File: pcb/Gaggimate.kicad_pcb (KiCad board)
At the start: 2 copper layers, 85 x 67 mm, 107 parts, among them J1 USB_C_Receptacle, J10 Conn_01x02, J2 Conn_01x02, J3 Conn_01x03, J4 Conn_01x04, J5 Conn_01x04, J6 Conn_01x10, J7 Conn_01x02, J8 Conn_01x02, J9 Conn_01x04, K1 Relay_SPDT, K2 Relay_SPDT, K3 Relay_SPDT, Q1 MMBT2222A, Q2 MMBT2222A, Q3 MMBT2222A, SW1 SW_Push, SW2 SW_Push, U1 ESP32-S3-WROOM-1, U2 AMS1117-3.3, U3 USBLC6-2SC6, U6 MAX31855EASA

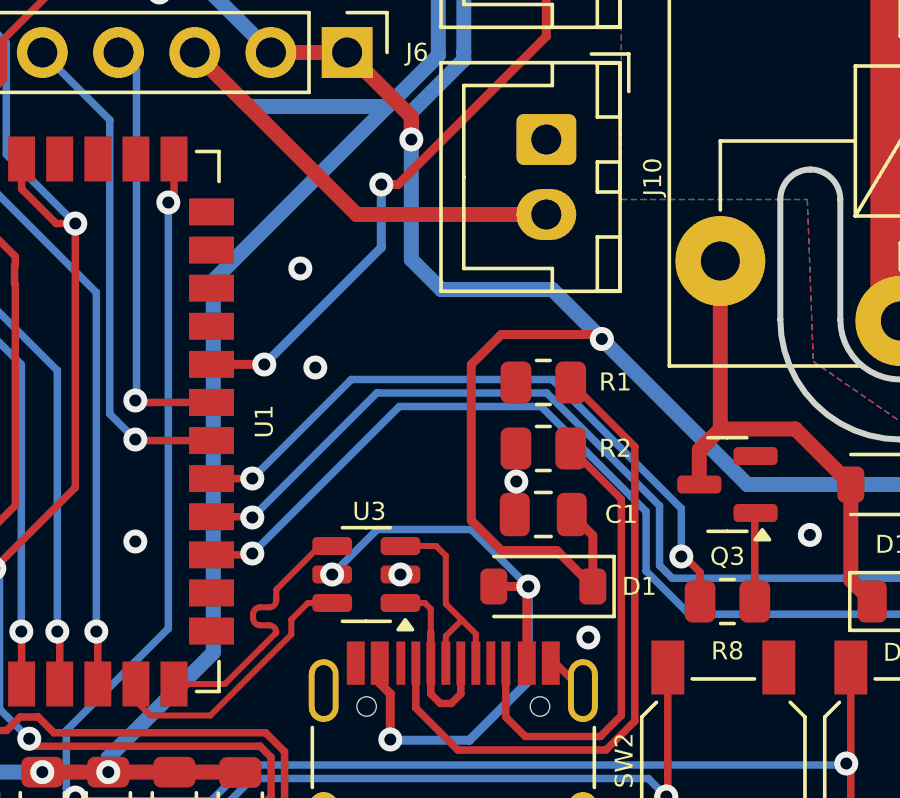
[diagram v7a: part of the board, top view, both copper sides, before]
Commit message: feat: Add expansion mounting hole to PCB, add expansion template
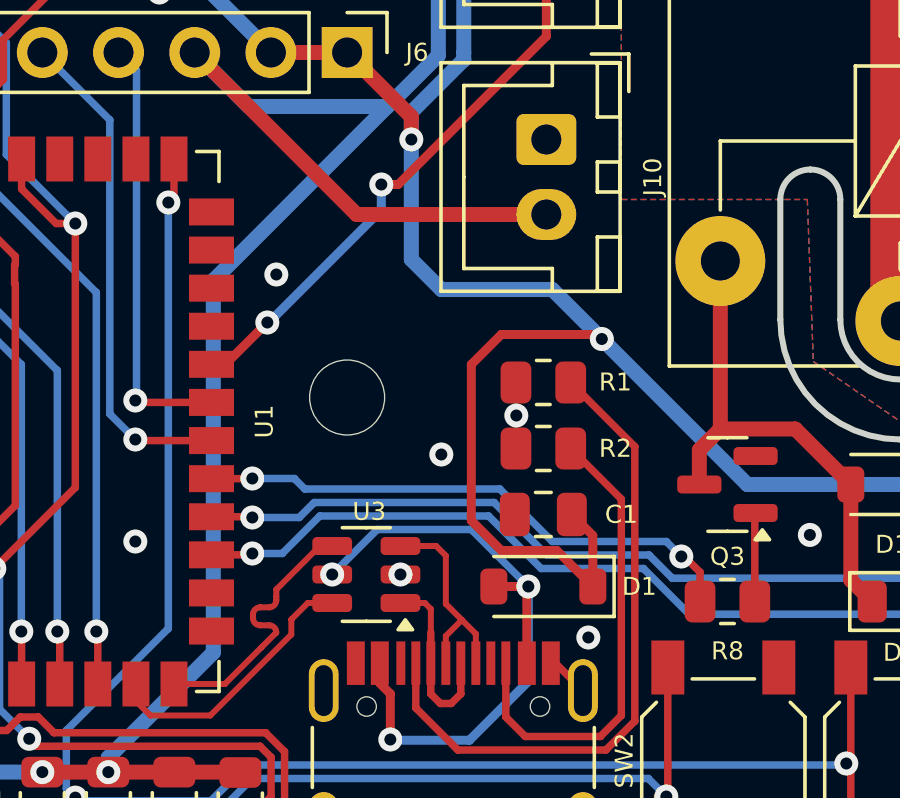
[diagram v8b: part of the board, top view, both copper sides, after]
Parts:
- added REF**: MountingHole_2.5mm, MountingHole:MountingHole_2.5mm, F.Cu at (186.9, 76.6)
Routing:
- net /RELAY_PUMP: track 57.1 -> 53.0 mm
- net /RELAY_VALVE: track 39.6 -> 35.4 mm
- net /RELAY_GRINDER: track 22.3 -> 18.7 mm
- net /SSR: track 19.8 -> 19.0 mm
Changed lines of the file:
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@@
 	(net 71 "unconnected-(D6-K-Pad1)")
 	(net 72 "Net-(K1-PadA1)")
+	(footprint "MountingHole:MountingHole_2.5mm"
+		(layer "F.Cu")
+		(at 186.86 76.6)
+		(descr "Mounting Hole 2.5mm, no annular")
+		(tags "mounting hole 2.5mm no annular")
+		(property "Reference" "REF**"
+			(at 0 -3.5 0)
+			(layer "F.SilkS")
+			(hide yes)
+			(effects
+				(font
+					(size 1 1)
+					(thickness 0.15)
+				)
+			)
+		)
+		(property "Value" "MountingHole_2.5mm"
+			(at 0 3.5 0)
+			(layer "F.Fab")
+			(hide yes)
+			(effects
+				(font
+					(size 1 1)
+					(thickness 0.15)
+				)
+			)
+		)
+		(property "Footprint" "MountingHole:MountingHole_2.5mm"
+			(at 0 0 0)
+			(unlocked yes)
+			(layer "F.Fab")
+			(hide yes)
+			(effects
+				(font
+					(size 1.27 1.27)
+					(thickness 0.15)
+				)
+			)
+		)
+		(property "Datasheet" ""
+			(at 0 0 0)
+			(unlocked yes)
+			(layer "F.Fab")
+			(hide yes)
+			(effects
+				(font
+					(size 1.27 1.27)
+					(thickness 0.15)
+				)
+			)
+		)
+		(property "Description" ""
+			(at 0 0 0)
+			(unlocked yes)
+			(layer "F.Fab")
+			(hide yes)
+			(effects
+				(font
+					(size 1.27 1.27)
+					(thickness 0.15)
+				)
+			)
+		)
+		(attr exclude_from_pos_files exclude_from_bom)
+		(fp_circle
+			(center 0 0)
+			(end 2.75 0)
+			(stroke
+				(width 0.05)
+				(type solid)
+			)
+			(fill none)
+			(layer "F.CrtYd")
+		)
+		(fp_text user "${REFERENCE}"
+			(at 0 0 0)
+			(layer "F.Fab")
+			(effects
+				(font
+					(size 1 1)
+					(thickness 0.15)
+				)
+			)
+		)
+		(pad "" np_thru_hole circle
+			(at 0 0)
+			(size 2.5 2.5)
+			(drill 2.5)
+			(layers "*.Cu" "*.Mask")
+		)
+	)
 	(footprint "Button_Switch_SMD:SW_SPST_SKQG_WithStem"
 		(layer "F.Cu")
@@
 			)
 		)
+		(property "LCSC" "C916372"
+			(at 0 0 180)
+			(unlocked yes)
+			(layer "F.Fab")
+			(hide yes)
+			(effects
+				(font
+					(size 1 1)
+					(thickness 0.15)
+				)
+			)
+		)
 		(property ki_fp_filters "SOT?23*")
 		(sheetname "Root")
@@
 			)
 		)
+		(property "LCSC" "C916372"
+			(at 0 0 180)
+			(unlocked yes)
+			(layer "F.Fab")
+			(hide yes)
+			(effects
+				(font
+					(size 1 1)
+					(thickness 0.15)
+				)
+			)
+		)
 		(property ki_fp_filters "SOT?23*")
 		(sheetname "Root")
@@
 			)
 		)
+		(property "LCSC" "C916372"
+			(at 0 0 180)
+			(unlocked yes)
+			(layer "F.Fab")
+			(hide yes)
+			(effects
+				(font
+					(size 1 1)
+					(thickness 0.15)
+				)
+			)
+		)
 		(property ki_fp_filters "SOT?23*")
 		(sheetname "Root")
@@
 	)
 	(via
-		(at 192.5 79.4)
+		(at 192.5 77.2)
 		(size 0.8)
 		(drill 0.4)
@@
 	)
 	(via
-		(at 185.8 75.6)
+		(at 190 78.5)
 		(size 0.8)
 		(drill 0.4)
@@
 	)
 	(via
-		(at 185.3 72.3)
+		(at 184.5 72.5)
 		(size 0.8)
 		(drill 0.4)
@@
 	)
 	(segment
-		(start 198.263299 83.825)
-		(end 228.775 83.825)
+		(start 228.775 83.825)
+		(end 230.7 81.9)
 		(width 0.25)
 		(layer "B.Cu")
@@
 	)
 	(segment
-		(start 196.825 80.397792)
-		(end 196.825 82.386701)
+		(start 183.7 81.8)
+		(end 184.7 81.8)
 		(width 0.25)
 		(layer "B.Cu")
@@
 	)
 	(segment
-		(start 188.6 76.9)
-		(end 193.327208 76.9)
+		(start 184.7 81.8)
+		(end 185.95 80.55)
 		(width 0.25)
 		(layer "B.Cu")
@@
 	)
 	(segment
-		(start 193.327208 76.9)
-		(end 196.825 80.397792)
+		(start 198.263299 83.825)
+		(end 228.775 83.825)
 		(width 0.25)
 		(layer "B.Cu")
@@
 	)
 	(segment
-		(start 183.7 81.8)
-		(end 188.6 76.9)
+		(start 191.575305 80.55)
+		(end 193.325305 82.3)
 		(width 0.25)
 		(layer "B.Cu")
@@
 	)
 	(segment
-		(start 196.825 82.386701)
+		(start 196.738299 82.3)
 		(end 198.263299 83.825)
 		(width 0.25)
@@
 	)
 	(segment
-		(start 228.775 83.825)
-		(end 230.7 81.9)
+		(start 185.95 80.55)
+		(end 191.575305 80.55)
+		(width 0.25)
+		(layer "B.Cu")
+		(net 23)
+	)
+	(segment
+		(start 193.325305 82.3)
+		(end 196.738299 82.3)
 		(width 0.25)
 		(layer "B.Cu")
@@
 	)
 	(segment
-		(start 197.275 80.211396)
-		(end 197.275 82.200305)
+		(start 197.699695 82.625)
+		(end 213.675 82.625)
 		(width 0.25)
 		(layer "B.Cu")
@@
 	)
 	(segment
-		(start 213.675 82.625)
-		(end 214.4 81.9)
+		(start 193.511701 81.85)
+		(end 196.924695 81.85)
 		(width 0.25)
 		(layer "B.Cu")
@@
 	)
 	(segment
-		(start 183.7 80.6)
-		(end 187.85 76.45)
+		(start 191.761701 80.1)
+		(end 193.511701 81.85)
 		(width 0.25)
 		(layer "B.Cu")
@@
 	)
 	(segment
-		(start 197.275 82.200305)
-		(end 197.699695 82.625)
+		(start 185.263604 80.6)
+		(end 185.763604 80.1)
 		(width 0.25)
 		(layer "B.Cu")
@@
 	)
 	(segment
-		(start 187.85 76.45)
-		(end 193.513604 76.45)
+		(start 185.763604 80.1)
+		(end 191.761701 80.1)
 		(width 0.25)
 		(layer "B.Cu")
@@
 	)
 	(segment
-		(start 193.513604 76.45)
-		(end 197.275 80.211396)
+		(start 183.7 80.6)
+		(end 185.263604 80.6)
 		(width 0.25)
 		(layer "B.Cu")
@@
 	)
 	(segment
-		(start 197.699695 82.625)
-		(end 213.675 82.625)
+		(start 213.675 82.625)
+		(end 214.4 81.9)
+		(width 0.25)
+		(layer "B.Cu")
+		(net 26)
+	)
+	(segment
+		(start 196.924695 81.85)
+		(end 197.699695 82.625)
 		(width 0.25)
 		(layer "B.Cu")
@@
 	)
 	(segment
-		(start 183.7 79.3)
-		(end 187 76)
+		(start 191.948097 79.65)
+		(end 193.698097 81.4)
 		(width 0.25)
 		(layer "B.Cu")
@@
 	)
 	(segment
-		(start 193.7 76)
-		(end 198 80.3)
+		(start 193.698097 81.4)
+		(end 197.5 81.4)
 		(width 0.25)
 		(layer "B.Cu")
@@
 	)
 	(segment
-		(start 187 76)
-		(end 193.7 76)
+		(start 197.5 81.4)
+		(end 198 81.9)
 		(width 0.25)
 		(layer "B.Cu")
@@
 	)
 	(segment
-		(start 198 80.3)
-		(end 198 81.9)
+		(start 183.7 79.3)
+		(end 185.1 79.3)
+		(width 0.25)
+		(layer "B.Cu")
+		(net 27)
+	)
+	(segment
+		(start 185.45 79.65)
+		(end 191.948097 79.65)
+		(width 0.25)
+		(layer "B.Cu")
+		(net 27)
+	)
+	(segment
+		(start 185.1 79.3)
+		(end 185.45 79.65)
 		(width 0.25)
 		(layer "B.Cu")
@@
 	)
 	(segment
-		(start 184.095 75.495)
-		(end 184.1 75.5)
-		(width 0.25)
+		(start 193.5 64.560661)
+		(end 193.5 61.7)
+		(width 0.3)
 		(layer "F.Cu")
 		(net 30)
@@
 	(segment
 		(start 182.34 75.495)
-		(end 184.095 75.495)
+		(end 182.805 75.495)
 		(width 0.3)
 		(layer "F.Cu")
@@
 	)
 	(segment
-		(start 193.5 64.560661)
-		(end 193.5 61.7)
+		(start 188 69.5)
+		(end 188.560661 69.5)
 		(width 0.3)
 		(layer "F.Cu")
@@
 	)
 	(segment
-		(start 188 69.5)
-		(end 188.560661 69.5)
+		(start 182.805 75.495)
+		(end 184.2 74.1)
 		(width 0.3)
 		(layer "F.Cu")
@@
 	)
 	(via
-		(at 184.1 75.5)
+		(at 184.2 74.1)
 		(size 0.8)
 		(drill 0.4)
@@
 	)
 	(segment
-		(start 188 69.5)
-		(end 188 71.6)
+		(start 184.2 74.1)
+		(end 184.25 74.1)
+		(width 0.3)
+		(layer "B.Cu")
+		(net 30)
+	)
+	(segment
+		(start 188 70.35)
+		(end 188 69.5)
 		(width 0.3)
 		(layer "B.Cu")
@@
 	)
 	(segment
-		(start 188 71.6)
-		(end 184.1 75.5)
+		(start 184.25 74.1)
+		(end 188 70.35)
 		(width 0.3)
 		(layer "B.Cu")
